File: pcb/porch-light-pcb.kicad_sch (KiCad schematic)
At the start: 11 parts, among them J1 1-2834011-3, J2 Conn_01x02, K1 PRY2-3V-450-1A-EF, Q1 PN2222A

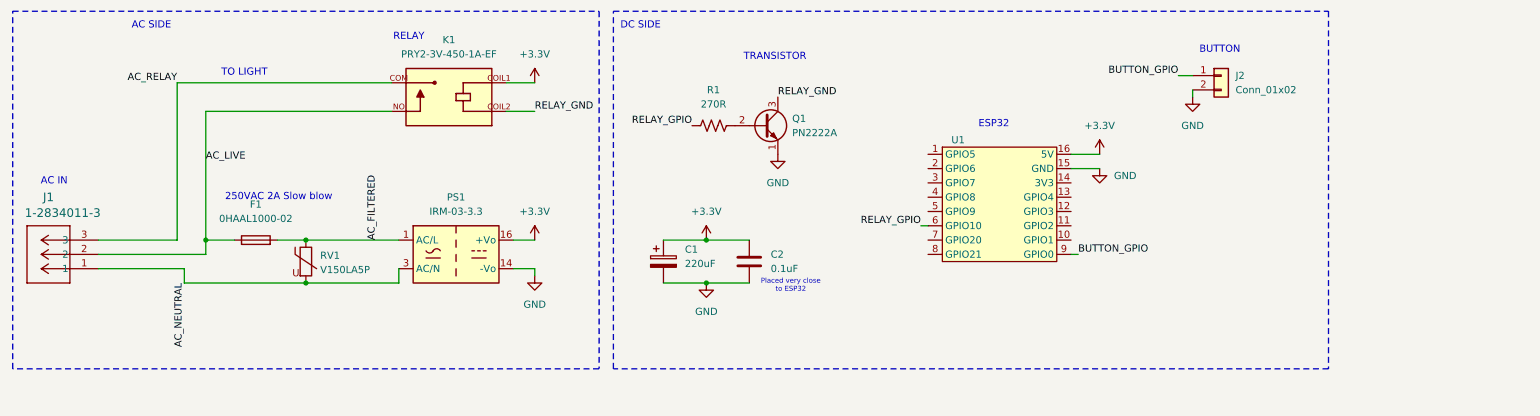
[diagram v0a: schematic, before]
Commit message: added flyback diode to relay
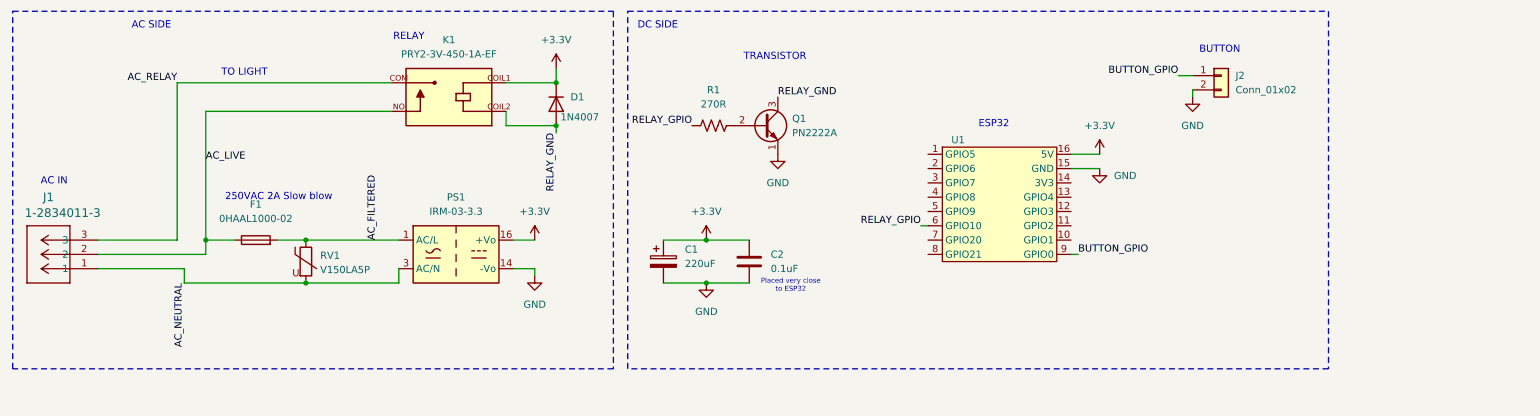
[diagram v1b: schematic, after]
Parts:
- added D1: 1N4007, Diode_SMD:D_SOD-123F, symbol Diode:1N4007
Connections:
- net +3.3V: now also D1.1 (K)
- net RELAY_GND: now also D1.2 (A)
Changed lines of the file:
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@@
 	(paper "A4")
 	(rectangle
-		(start 120.65 13.97)
+		(start 123.19 13.97)
 		(end 247.65 77.47)
 		(stroke
@@
 	(rectangle
 		(start 13.97 13.97)
-		(end 118.11 77.47)
+		(end 120.65 77.47)
 		(stroke
 			(width 0)
@@
 	(text "DC SIDE\n"
 		(exclude_from_sim no)
-		(at 125.476 16.51 0)
+		(at 128.524 16.51 0)
 		(effects
 			(font
@@
 			)
 		)
+	)
+	(junction
+		(at 110.49 26.67)
+		(diameter 0)
+		(color 0 0 0 0)
 	)
 	(junction
@@
 	)
 	(junction
+		(at 110.49 34.29)
+		(diameter 0)
+		(color 0 0 0 0)
+	)
+	(junction
 		(at 48.26 54.61)
 		(diameter 0)
@@
 	(wire
 		(pts
+			(xy 101.6 34.29) (xy 101.6 31.75)
+		)
+		(stroke
+			(width 0)
+			(type default)
+		)
+	)
+	(wire
+		(pts
 			(xy 29.21 57.15) (xy 48.26 57.15)
 		)
@@
 	(wire
 		(pts
-			(xy 101.6 26.67) (xy 106.68 26.67)
+			(xy 101.6 34.29) (xy 110.49 34.29)
+		)
+		(stroke
+			(width 0)
+			(type default)
+		)
+	)
+	(wire
+		(pts
+			(xy 101.6 26.67) (xy 110.49 26.67)
 		)
 		(stroke
@@
 	(wire
 		(pts
-			(xy 106.68 31.75) (xy 101.6 31.75)
+			(xy 110.49 34.29) (xy 110.49 35.56)
 		)
 		(stroke
@@
 		(pts
 			(xy 66.04 62.23) (xy 82.55 62.23)
+		)
+		(stroke
+			(width 0)
+			(type default)
+		)
+	)
+	(wire
+		(pts
+			(xy 110.49 24.13) (xy 110.49 26.67)
 		)
 		(stroke
@@
 		)
 	)
-	(label "RELAY_GND"
-		(at 106.68 31.75 0)
-		(effects
-			(font
-				(size 1.27 1.27)
-			)
-			(justify left bottom)
-		)
-	)
 	(label "RELAY_GPIO"
 		(at 175.26 52.07 180)
+		(effects
+			(font
+				(size 1.27 1.27)
+			)
+			(justify right bottom)
+		)
+	)
+	(label "RELAY_GND"
+		(at 110.49 35.56 270)
 		(effects
 			(font
@@
 	)
 	(symbol
+		(lib_id "Diode:1N4007")
+		(at 110.49 30.48 270)
+		(unit 1)
+		(exclude_from_sim no)
+		(in_bom yes)
+		(on_board yes)
+		(dnp no)
+		(property "Reference" "D1"
+			(at 113.03 29.2099 90)
+			(effects
+				(font
+					(size 1.27 1.27)
+				)
+				(justify left)
+			)
+		)
+		(property "Value" "1N4007"
+			(at 111.252 32.766 90)
+			(effects
+				(font
+					(size 1.27 1.27)
+				)
+				(justify left)
+			)
+		)
+		(property "Footprint" "Diode_SMD:D_SOD-123F"
+			(at 106.045 30.48 0)
+			(effects
+				(font
+					(size 1.27 1.27)
+				)
+				(hide yes)
+			)
+		)
+		(property "Datasheet" "http://www.vishay.com/docs/88503/1n4001.pdf"
+			(at 110.49 30.48 0)
+			(effects
+				(font
+					(size 1.27 1.27)
+				)
+				(hide yes)
+			)
+		)
+		(property "Description" "1000V 1A General Purpose Rectifier Diode, DO-41"
+			(at 110.49 30.48 0)
+			(effects
+				(font
+					(size 1.27 1.27)
+				)
+				(hide yes)
+			)
+		)
+		(property "Sim.Device" "D"
+			(at 110.49 30.48 0)
+			(effects
+				(font
+					(size 1.27 1.27)
+				)
+				(hide yes)
+			)
+		)
+		(property "Sim.Pins" "1=K 2=A"
+			(at 110.49 30.48 0)
+			(effects
+				(font
+					(size 1.27 1.27)
+				)
+				(hide yes)
+			)
+		)
+		(pin "2"
+		)
+		(pin "1"
+		)
+		(instances
+			(project "porch-light-pcb"
+				(path "/c90725bf-bd5a-4426-8225-f7c4cfb17e78"
+					(reference "D1")
+					(unit 1)
+				)
+			)
+		)
+	)
+	(symbol
 		(lib_id "power:+3.3V")
 		(at 137.16 54.61 0)
@@
 	(symbol
 		(lib_id "power:+3.3V")
-		(at 106.68 26.67 0)
+		(at 110.49 24.13 0)
 		(unit 1)
 		(exclude_from_sim no)
@@
 		(fields_autoplaced yes)
 		(property "Reference" "#PWR09"
-			(at 106.68 30.48 0)
+			(at 110.49 27.94 0)
 			(effects
 				(font
@@
 		)
 		(property "Value" "+3.3V"
-			(at 106.68 21.59 0)
+			(at 110.49 19.05 0)
 			(effects
 				(font
@@
 		)
 		(property "Footprint" ""
-			(at 106.68 26.67 0)
+			(at 110.49 24.13 0)
 			(effects
 				(font
@@
 		)
 		(property "Datasheet" ""
-			(at 106.68 26.67 0)
+			(at 110.49 24.13 0)
 			(effects
 				(font
@@
 		)
 		(property "Description" "Power symbol creates a global label with name \"+3.3V\""
-			(at 106.68 26.67 0)
-			(effects
-				(font
+			(at 110.49 24.13 0)
+			(effects
+				(font

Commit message: swapped 220uF for 47uF, added jumper to disable USB power
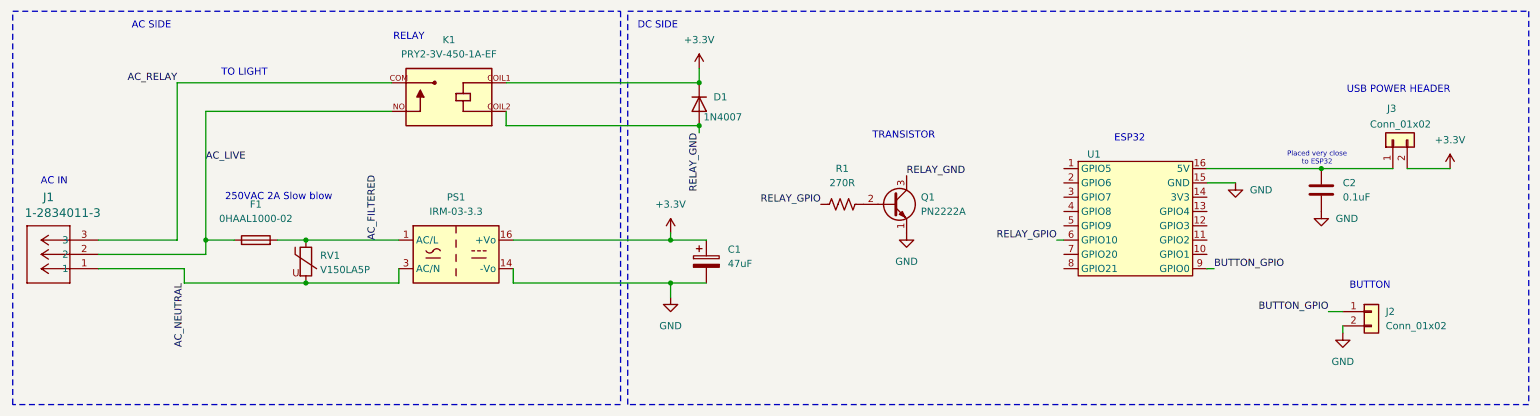
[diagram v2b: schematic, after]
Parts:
- added J3: Conn_01x02, Connector_PinHeader_2.54mm:PinHeader_1x02_P2.54mm_Vertical, symbol Connector_Generic:Conn_01x02
- C1: value 220uF -> 47uF; footprint Capacitor_THT:CP_Radial_D5.0mm_P2.50mm -> Capacitor_THT:CP_Radial_D4.0mm_P1.50mm
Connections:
- net +3.3V: now also J3.2 (Pin_2); no longer C2.1, U1.16 (5V)
- net GND: now also C2.1; no longer C2.2
- new net: C2.2, J3.1 (Pin_1), U1.16 (5V)
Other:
- note added: "USB POWER HEADER"
- moved on the sheet: C1, C2, D1, J2, Q1, R1, U1
